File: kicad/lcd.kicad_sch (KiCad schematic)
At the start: 6 parts, among them J7 R61529 LCD, J8 FT6236, Q4 DMN2004WK-7

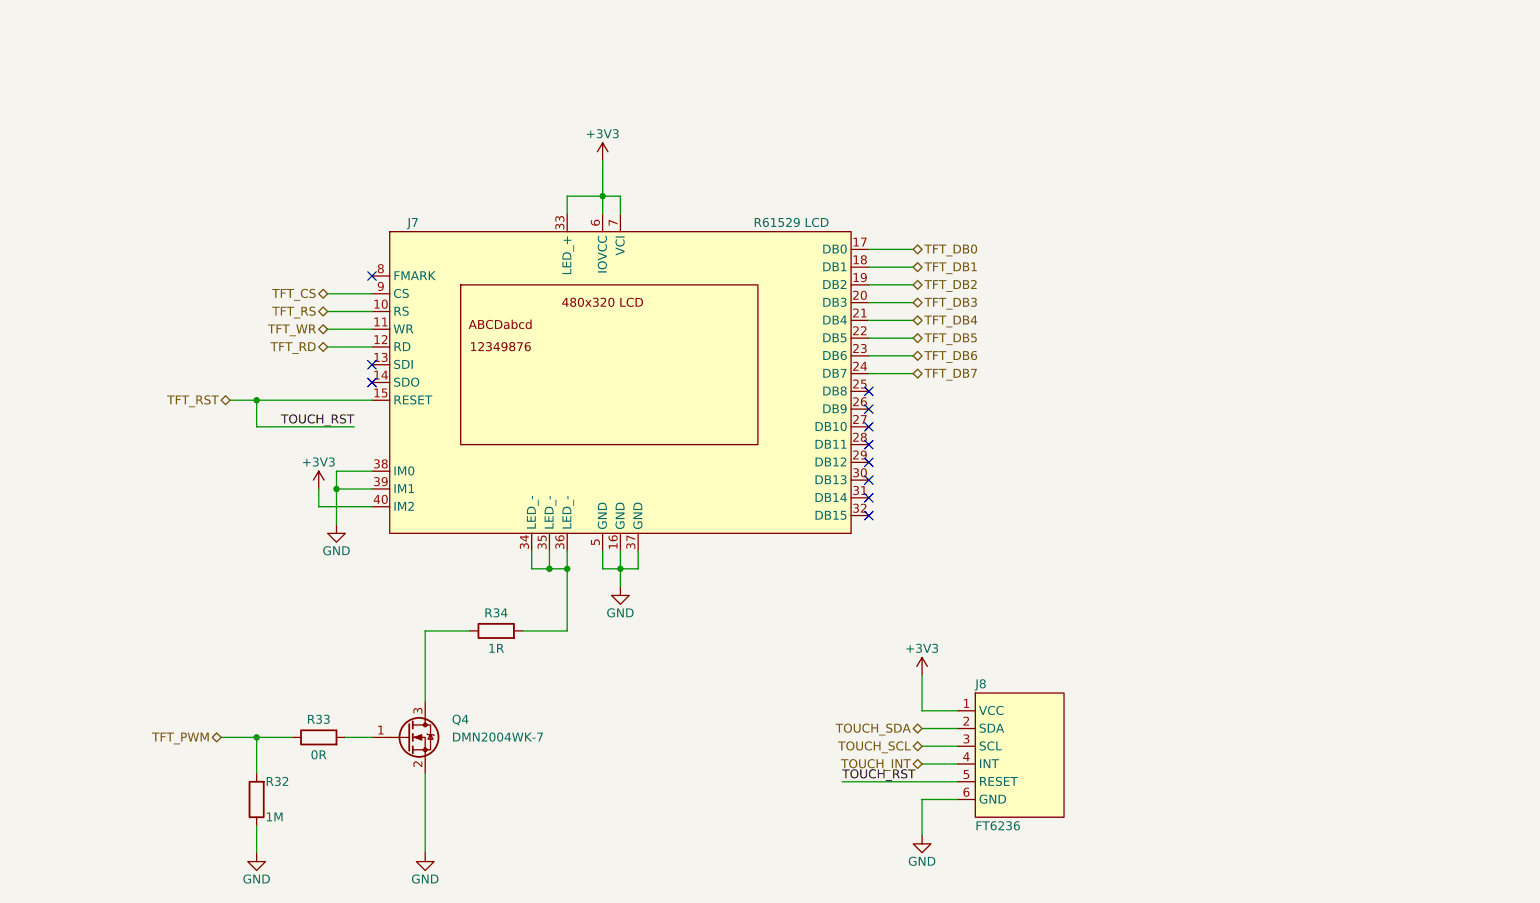
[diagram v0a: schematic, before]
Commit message: refactor KiCAD Project to v6
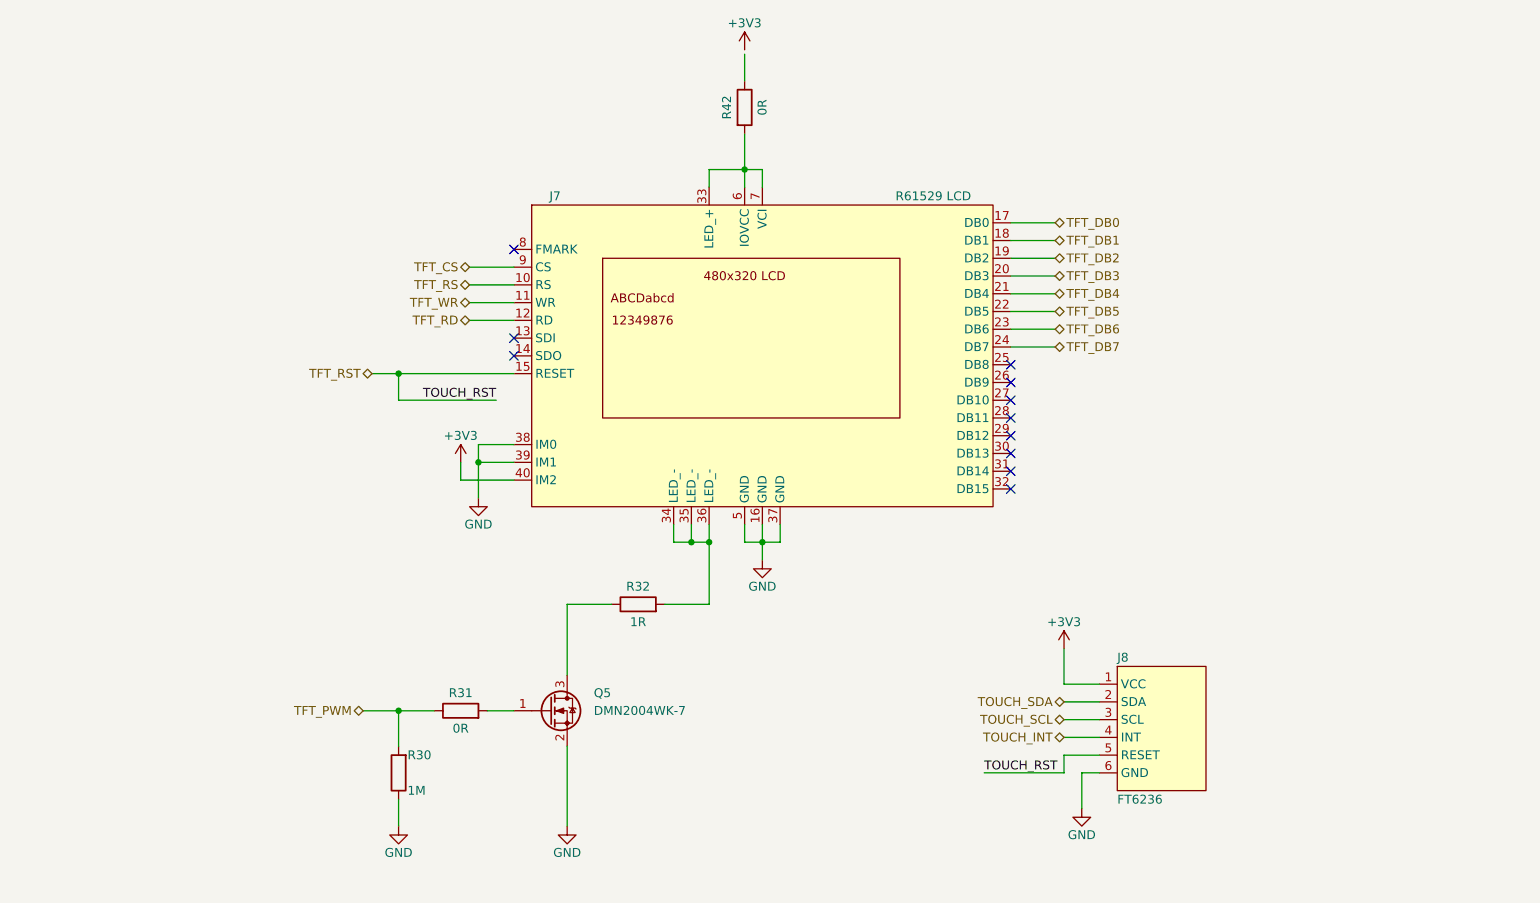
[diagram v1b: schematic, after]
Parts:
- removed Q4: DMN2004WK-7, Package_TO_SOT_SMD:SOT-323_SC-70, symbol z_ic:DMN2004WK-7
- removed R33: 0R, Resistor_SMD:R_0603_1608Metric, symbol Device:R
- removed R34: 1R, Resistor_SMD:R_0805_2012Metric, symbol Device:R
- added Q5: DMN2004WK-7, Package_TO_SOT_SMD:SOT-323_SC-70, symbol z_ic:DMN2004WK-7
- added R30: 1M, Resistor_SMD:R_0603_1608Metric, symbol Device:R
- added R31, R42: 0R, Resistor_SMD:R_0603_1608Metric, symbol Device:R
- J7: Digikey (none) -> WM3431CT-ND
- J8: Digikey (none) -> 609-4332-1-ND
- R32: value 1M -> 1R; footprint Resistor_SMD:R_0603_1608Metric -> Resistor_SMD:R_1206_3216Metric; Digikey YAG4498CT-ND -> CSR1206FT1R00CT-ND
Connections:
- net +3V3: no longer J7.33 (LED_+), J7.6 (IOVCC), J7.7 (VCI)
- net GND: now also Q5.2 (S), R30.1; no longer R32.1
- net TFT_PWM: now also R30.2, R31.1; no longer R32.2
- net at J7.34 (LED_-), J7.35 (LED_-), J7.36 (LED_-): now also R32.2
- new net: Q5.1 (G), R31.2
- new net: Q5.3 (D), R32.1
- new net: J7.33 (LED_+), J7.6 (IOVCC), J7.7 (VCI), R42.2

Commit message: add rules to .gitignore
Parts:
- removed J7: R61529 LCD, z_connector:62684-402100ALF, symbol z_ic:R61529 LCD
- removed J8: FT6236, z_connector:SFV6R-2STE1HLF, symbol z_ic:FT6236
- removed Q5: DMN2004WK-7, Package_TO_SOT_SMD:SOT-323_SC-70, symbol z_ic:DMN2004WK-7
- removed R30: 1M, Resistor_SMD:R_0603_1608Metric, symbol Device:R
- removed R31: 0R, Resistor_SMD:R_0603_1608Metric, symbol Device:R
- removed R32: 1R, Resistor_SMD:R_1206_3216Metric, symbol Device:R
- added J?: MIKROE-2168, z_connector:FPC_BOTTOM_20POS_Würth_68712014522, symbol z_ic:MIKROE-2168
- R?: renamed from R42; value 0R -> R
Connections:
- net +3V3: now also R?.1
- net GND: now also J?.19 (BLGND), J?.2 (GND), J?.20 (BLGND), J?.9 (MODE)
- net at R?.2: now also J?.1 (VDD), J?.17 (BLVDD), J?.18 (BLVDD)
- new net: J?.11, J?.12, J?.13, J?.14, J?.15, J?.16
- new net SPI_MISO: J?.4 (SPI_MISO)
- new net SPI_MOSI: J?.5 (SPI_MOSI)
- new net SPI_SCLK: J?.3 (SPI_SCLK)
- new net SPI_~{CS}: J?.6 (SPI_CS)
- new net ~{INT}: J?.7 (~{INT})
- new net ~{PD}: J?.8 (~{PD})
- no-connect marks 11 -> 1
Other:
- moved on the sheet: R?

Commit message: add connection to lcd
import parts into pcbnew
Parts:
- J7: renamed from J?; value MIKROE-2168 -> R61529 LCD; footprint z_connector:FPC_BOTTOM_20POS_Würth_68712014522 -> z_connector:62684-402100ALF
- R42: renamed from R?; value R -> 0R
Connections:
- now unconnected: J7.11, J7.12, J7.13, J7.14, J7.15, J7.16
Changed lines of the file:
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@@
     (effects (font (size 1.27 1.27)) (justify right))
   )
-  (hierarchical_label "~{INT}" (shape input) (at 95.25 81.28 180)
+  (hierarchical_label "~{INT}" (shape output) (at 95.25 81.28 180)
     (effects (font (size 1.27 1.27)) (justify right))
   )
@@
   )
   (symbol (lib_id "z_ic:MIKROE-2168") (at 137.16 74.93 0) (unit 1)
-    (in_bom yes) (on_board yes) (fields_autoplaced)
-    (property "Reference" "J?" (id 0) (at 173.99 73.6599 0)
+    (in_bom yes) (on_board yes)
+    (property "Reference" "J7" (id 0) (at 151.13 48.26 0)
       (effects (font (size 1.27 1.27)) (justify left))
     )
-    (property "Value" "MIKROE-2168" (id 1) (at 173.99 76.1999 0)
+    (property "Value" "R61529 LCD" (id 1) (at 151.13 50.8 0)
       (effects (font (size 1.27 1.27)) (justify left))
     )
-    (property "Footprint" "z_connector:FPC_BOTTOM_20POS_Würth_68712014522" (id 2) (at 122.555 69.215 0)
+    (property "Footprint" "z_connector:62684-402100ALF" (id 2) (at 122.555 69.215 0)
       (effects (font (size 1.27 1.27)) hide)
     )
@@
   (symbol (lib_id "power:GND") (at 137.16 109.22 0) (unit 1)
     (in_bom yes) (on_board yes) (fields_autoplaced)
-    (property "Reference" "#PWR?" (id 0) (at 137.16 115.57 0)
+    (property "Reference" "#PWR0154" (id 0) (at 137.16 115.57 0)
       (effects (font (size 1.27 1.27)) hide)
     )
@@
   (symbol (lib_id "power:+3V3") (at 137.16 31.75 0) (unit 1)
     (in_bom yes) (on_board yes)
-    (property "Reference" "#PWR?" (id 0) (at 137.16 35.56 0)
+    (property "Reference" "#PWR0158" (id 0) (at 137.16 35.56 0)
       (effects (font (size 1.27 1.27)) hide)
     )
@@
   (symbol (lib_id "power:GND") (at 95.25 92.71 0) (unit 1)
     (in_bom yes) (on_board yes) (fields_autoplaced)
-    (property "Reference" "#PWR?" (id 0) (at 95.25 99.06 0)
+    (property "Reference" "#PWR0140" (id 0) (at 95.25 99.06 0)
       (effects (font (size 1.27 1.27)) hide)
     )
@@
   (symbol (lib_id "Device:R") (at 137.16 39.37 0) (unit 1)
     (in_bom yes) (on_board yes)
-    (property "Reference" "R?" (id 0) (at 134.62 39.37 90))
-    (property "Value" "R" (id 1) (at 139.7 39.37 90))
+    (property "Reference" "R42" (id 0) (at 134.62 39.37 90))
+    (property "Value" "0R" (id 1) (at 139.7 39.37 90))
     (property "Footprint" "Resistor_SMD:R_0603_1608Metric" (id 2) (at 135.382 39.37 90)
       (effects (font (size 1.27 1.27)) hide)

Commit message: route complete pcb
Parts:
- J8: renamed from J7; footprint z_connector:62684-402100ALF -> z_connector:FPC_BOTTOM_20POS_Würth_68712014522
- renumbered R42 to R34
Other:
- moved on the sheet: J8, R34

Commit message: rework pcb
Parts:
- removed J8: R61529 LCD, z_connector:FPC_BOTTOM_20POS_Würth_68712014522, symbol z_ic:MIKROE-2168
- added J8: RVT50HQBNWC00, mylib_connector:FPC_BOTTOM_20POS_Würth_68712014522, symbol mylib_ic:RVT50HQBNWC00
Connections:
- net GND: now also J8.19 (BLGND), J8.2 (GND), J8.20 (BLGND)
- net ~{INT}: now also J8.7 (~{INT})
- net ~{PD}: now also J8.8 (~{PD})
- net at R34.2: now also J8.1 (VDD), J8.17 (BLVDD), J8.18 (BLVDD)
- new net GPIO0.0: J8.9 (GPIO0.0)
- new net QSPI_IO.0: J8.5 (MOSI/IO.0)
- new net QSPI_IO.1: J8.4 (MISO/IO.1)
- new net QSPI_IO.2: J8.11 (GPIO0.1/IO.2)
- new net QSPI_IO.3: J8.12 (GPIO0.2/IO.3)
- new net QSPI_SCLK: J8.3 (SCLK)
- new net QSPI_~{CS}: J8.6 (CS)
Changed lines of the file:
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@@
   (junction (at 137.16 71.12) (diameter 0) (color 0 0 0 0)
   )
-  (no_connect (at 101.6 111.76))
+  (no_connect (at 101.6 116.84))
+  (wire (pts (xy 95.25 93.98) (xy 101.6 93.98))
+    (stroke (width 0) (type default) (color 0 0 0 0))
+  )
   (wire (pts (xy 95.25 86.36) (xy 101.6 86.36))
     (stroke (width 0) (type default) (color 0 0 0 0))
@@
   )
   (wire (pts (xy 143.51 71.12) (xy 146.05 71.12))
-    (stroke (width 0) (type default) (color 0 0 0 0))
-  )
-  (wire (pts (xy 101.6 109.22) (xy 95.25 109.22))
     (stroke (width 0) (type default) (color 0 0 0 0))
   )
@@
     (stroke (width 0) (type default) (color 0 0 0 0))
   )
-  (wire (pts (xy 95.25 109.22) (xy 95.25 115.57))
-    (stroke (width 0) (type default) (color 0 0 0 0))
-  )
   (wire (pts (xy 95.25 106.68) (xy 101.6 106.68))
     (stroke (width 0) (type default) (color 0 0 0 0))
   )
   (wire (pts (xy 137.16 124.46) (xy 137.16 132.08))
+    (stroke (width 0) (type default) (color 0 0 0 0))
+  )
+  (wire (pts (xy 95.25 91.44) (xy 101.6 91.44))
     (stroke (width 0) (type default) (color 0 0 0 0))
   )
@@
     (stroke (width 0) (type default) (color 0 0 0 0))
   )
+  (wire (pts (xy 95.25 114.3) (xy 101.6 114.3))
+    (stroke (width 0) (type default) (color 0 0 0 0))
+  )
   (wire (pts (xy 146.05 121.92) (xy 146.05 124.46))
     (stroke (width 0) (type default) (color 0 0 0 0))
   )
-  (hierarchical_label "SPI_MISO" (shape bidirectional) (at 95.25 83.82 180)
+  (hierarchical_label "QSPI_IO.2" (shape bidirectional) (at 95.25 91.44 180)
+    (effects (font (size 1.27 1.27)) (justify right))
+  )
+  (hierarchical_label "QSPI_IO.1" (shape bidirectional) (at 95.25 86.36 180)
     (effects (font (size 1.27 1.27)) (justify right))
   )
@@
     (effects (font (size 1.27 1.27)) (justify right))
   )
-  (hierarchical_label "SPI_SCLK" (shape input) (at 95.25 81.28 180)
+  (hierarchical_label "QSPI_SCLK" (shape input) (at 95.25 83.82 180)
     (effects (font (size 1.27 1.27)) (justify right))
   )
-  (hierarchical_label "SPI_MOSI" (shape input) (at 95.25 86.36 180)
+  (hierarchical_label "QSPI_IO.3" (shape bidirectional) (at 95.25 93.98 180)
     (effects (font (size 1.27 1.27)) (justify right))
   )
-  (hierarchical_label "SPI_~{CS}" (shape input) (at 95.25 88.9 180)
+  (hierarchical_label "QSPI_IO.0" (shape bidirectional) (at 95.25 88.9 180)
     (effects (font (size 1.27 1.27)) (justify right))
   )
-  (symbol (lib_id "z_ic:MIKROE-2168") (at 137.16 97.79 0) (unit 1)
-    (in_bom yes) (on_board yes)
-    (property "Reference" "J8" (id 0) (at 151.13 71.12 0)
+  (hierarchical_label "QSPI_~{CS}" (shape input) (at 95.25 81.28 180)
+    (effects (font (size 1.27 1.27)) (justify right))
+  )
+  (hierarchical_label "GPIO0.0" (shape input) (at 95.25 114.3 180)
+    (effects (font (size 1.27 1.27)) (justify right))
+  )
+  (symbol (lib_id "mylib_ic:RVT50HQBNWC00") (at 137.16 97.79 0) (unit 1)
+    (in_bom yes) (on_board yes) (fields_autoplaced)
+    (property "Reference" "J8" (id 0) (at 171.45 95.2499 0)
       (effects (font (size 1.27 1.27)) (justify left))
     )
-    (property "Value" "R61529 LCD" (id 1) (at 151.13 73.66 0)
+    (property "Value" "RVT50HQBNWC00" (id 1) (at 171.45 97.7899 0)
       (effects (font (size 1.27 1.27)) (justify left))
     )
-    (property "Footprint" "z_connector:FPC_BOTTOM_20POS_Würth_68712014522" (id 2) (at 122.555 92.075 0)
+    (property "Footprint" "mylib_connector:FPC_BOTTOM_20POS_Würth_68712014522" (id 2) (at 125.095 92.075 0)
       (effects (font (size 1.27 1.27)) hide)
     )
-    (property "Datasheet" "https://download.mikroe.com/documents/datasheets/rvt43ulfnwc0x-rev.1.2.pdf" (id 3) (at 122.555 92.075 0)
+    (property "Datasheet" "https://download.mikroe.com/documents/datasheets/rvt43ulfnwc0x-rev.1.2.pdf" (id 3) (at 135.255 110.49 0)
       (effects (font (size 1.27 1.27)) hide)
     )
-    (property "Digikey" "1471-1711-ND" (id 4) (at 173.99 100.3299 0)
-      (effects (font (size 1.27 1.27)) (justify left) hide)
+    (property "Digikey" "1471-1711-ND" (id 4) (at 171.45 100.3299 0)
+      (effects (font (size 1.27 1.27)) (justify left))
     )
     (pin "1")
@@
       (effects (font (size 1.27 1.27)) hide)
     )
-    (pin "1")
-  )
-  (symbol (lib_id "power:GND") (at 95.25 115.57 0) (unit 1)
-    (in_bom yes) (on_board yes) (fields_autoplaced)
-    (property "Reference" "#PWR055" (id 0) (at 95.25 121.92 0)
-      (effects (font (size 1.27 1.27)) hide)
-    )
-    (property "Value" "GND" (id 1) (at 95.25 120.65 0))
-    (property "Footprint" "" (id 2) (at 95.25 115.57 0)
-      (effects (font (size 1.27 1.27)) hide)
-    )
-    (property "Datasheet" "" (id 3) (at 95.25 115.57 0)
-      (effects (font (size 1.27 1.27)) hide)
-    )

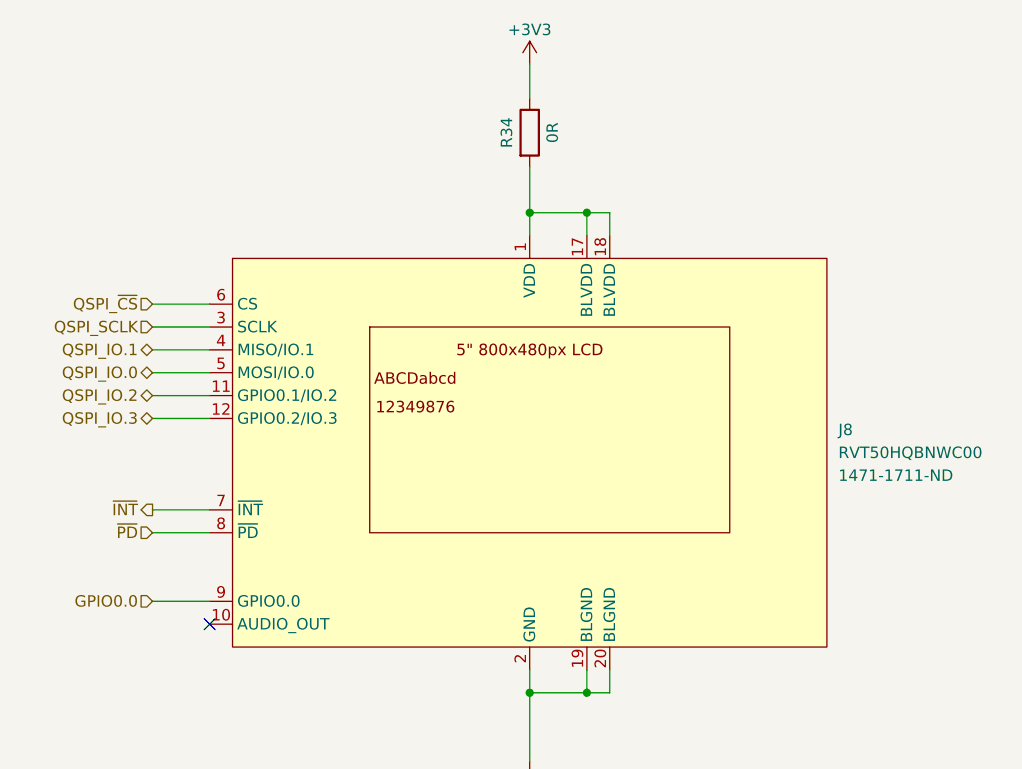
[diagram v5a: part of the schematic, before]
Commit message: add all digikeys numbers to schematic
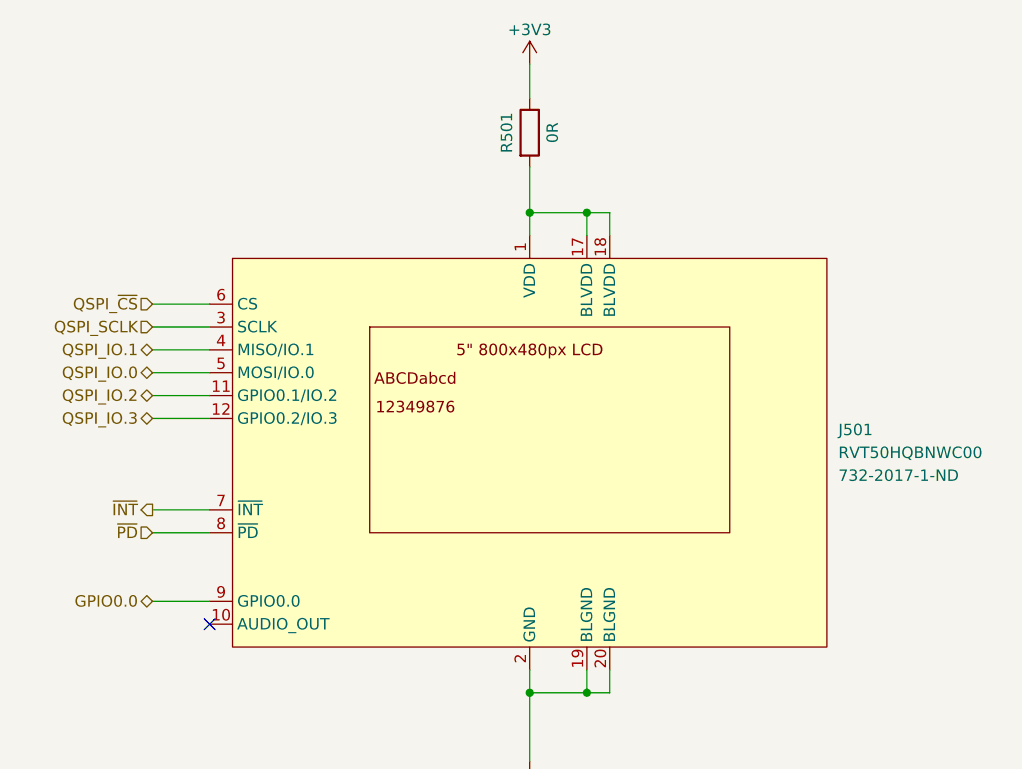
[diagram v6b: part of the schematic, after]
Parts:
- J501: renamed from J8; Digikey 1471-1711-ND -> 732-2017-1-ND
- renumbered R34 to R501
